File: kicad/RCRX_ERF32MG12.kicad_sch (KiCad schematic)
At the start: 90 parts, among them J20 USB_OTG, J21 USB, J22 USB, P10 LEDs, P6 SD Card, P9 BUZZ, SW1 SW_Push-switches, U1 MAX2650, U10 ATSAMD11D14A-M, U11 USB6B1, U12 MAX2650

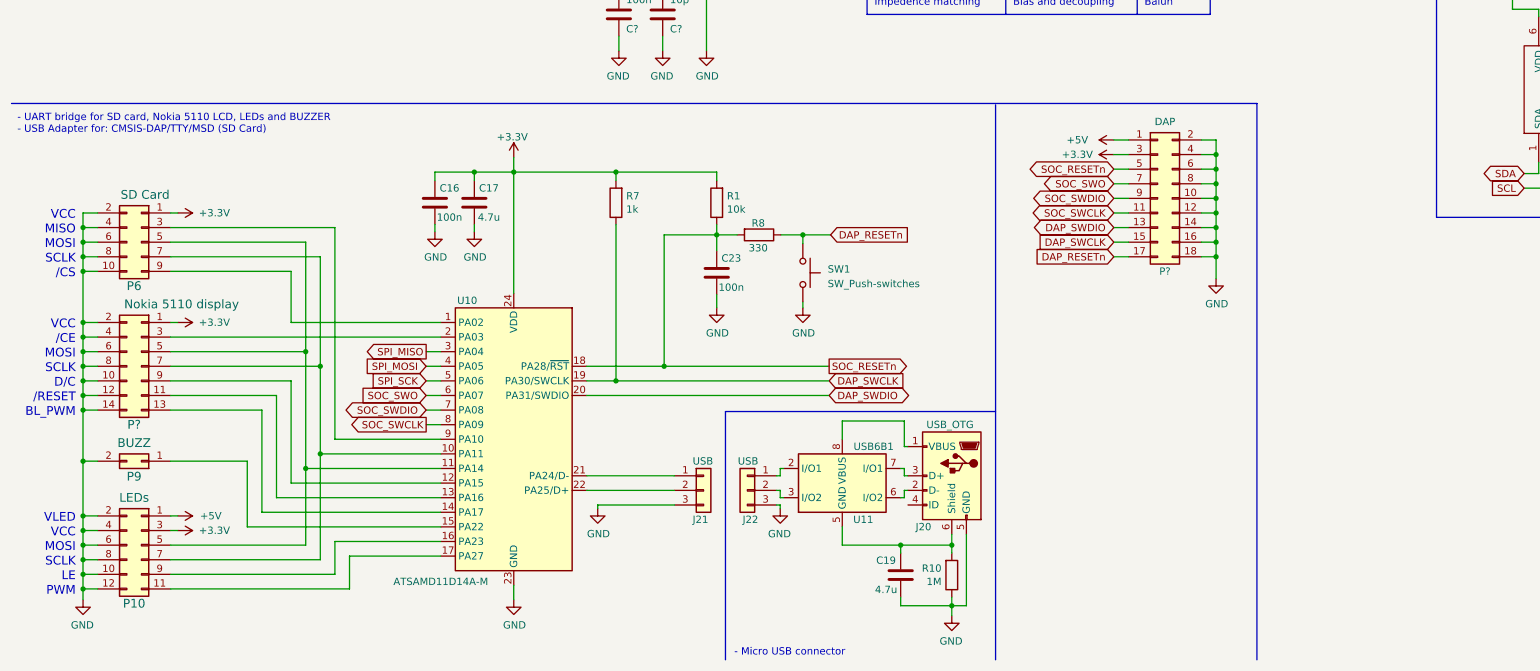
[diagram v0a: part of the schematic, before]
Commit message: Adding micro SD card slot in RX circuit
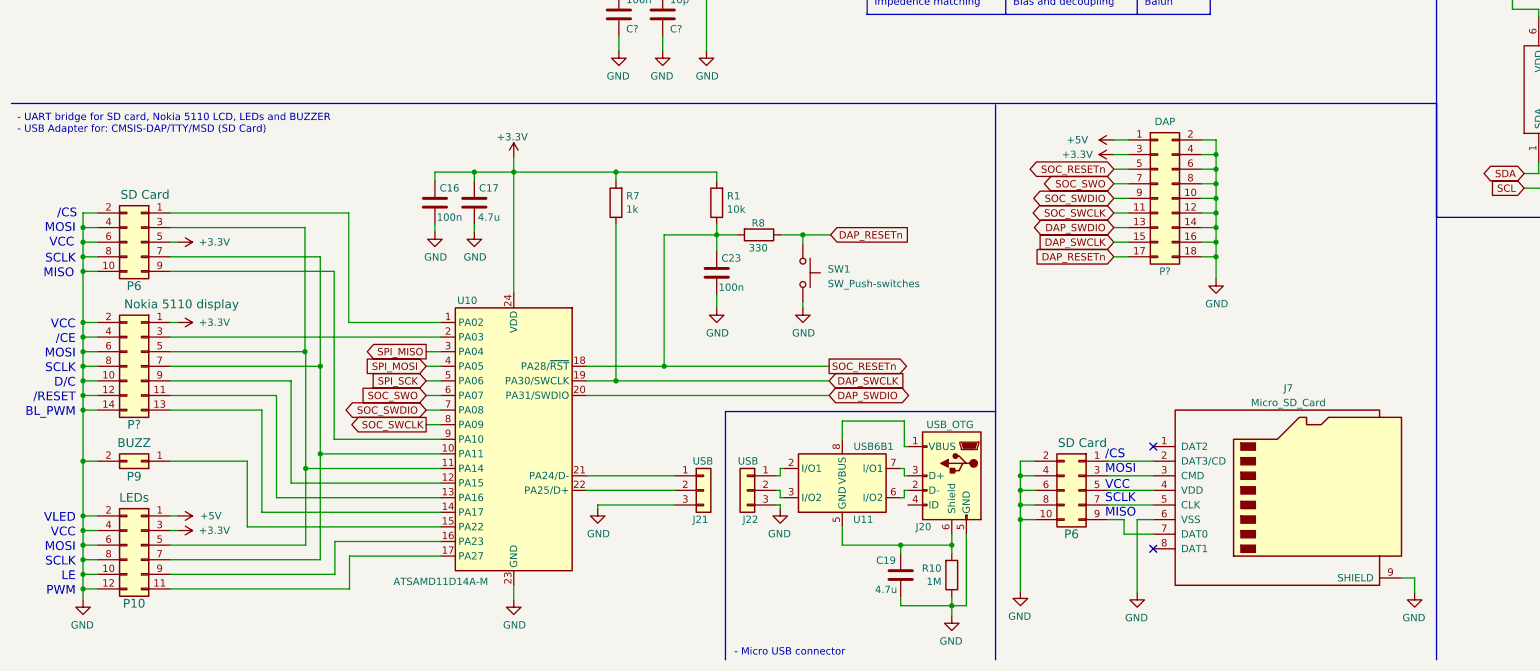
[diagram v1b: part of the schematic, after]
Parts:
- added J7: Micro_SD_Card, symbol Connector:Micro_SD_Card
- added P6: SD Card, symbol conn:Conn_02x05_Odd_Even
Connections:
- net +3V3: now also P6.5 (Pin_5); no longer P6.1 (Pin_1)
- net GND: now also J7.6 (VSS), J7.9 (SHIELD), P6.10 (Pin_10), P6.2 (Pin_2), P6.4 (Pin_4), P6.6 (Pin_6), P6.8 (Pin_8)
- net at U10.1 (PA02): now also P6.1 (Pin_1); no longer P6.9 (Pin_9)
- net at P10.5 (Pin_5), P?.5 (Pin_5), U10.11 (PA14): now also P6.3 (Pin_3); no longer P6.5 (Pin_5)
- net at U10.9 (PA10): now also P6.9 (Pin_9); no longer P6.3 (Pin_3)
- new net: J7.2 (DAT3/CD), P6.1 (Pin_1)
- new net: J7.3 (CMD), P6.3 (Pin_3)
- new net: J7.4 (VDD), P6.5 (Pin_5)
- new net: J7.5 (CLK), P6.7 (Pin_7)
- new net: J7.7 (DAT0), P6.9 (Pin_9)
- no-connect marks 11 -> 13

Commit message: Using EFM32HG310-QFN32 instead of SAMD11D14M for USB bridge - updating schematics
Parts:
- removed C23: 100n, symbol device:C
- removed J21, J22: USB, symbol Connector_Generic:Conn_01x03
- removed J7: Micro_SD_Card, symbol Connector:Micro_SD_Card
- removed P6 (x2): SD Card, symbol conn:Conn_02x05_Odd_Even
- removed P?: Nokia 5110 display, symbol Connector_Generic:Conn_02x07_Odd_Even
- removed R1: 10k, symbol device:R
- removed R7: 1k, symbol device:R
- removed R8: 330, symbol device:R
- removed U10: ATSAMD11D14A-M, Package_DFN_QFN:QFN-24-1EP_4x4mm_P0.5mm_EP2.6x2.6mm, symbol MCU_Microchip_SAMD:ATSAMD11D14A-M
- added C24, C32: 1u, symbol device:C
- added C25, C26: 10n, symbol device:C
- added C27, C28, C30: 0.1u, symbol device:C
- added C29, C31: 10u, symbol device:C
- added C33: 4.7u, symbol device:C
- added J11: Micro_SD_Card, symbol Connector:Micro_SD_Card
- added J21, J22: USB, symbol Connector_Generic:Conn_01x04
- added P?: Nokia 5110 display, symbol Connector_Generic:Conn_02x07_Odd_Even
- added U10: EFM32HG310F64G-C-QFN32, Package_DFN_QFN:QFN-32-1EP_6x6mm_P0.65mm_EP4.4x4.4mm, symbol EFM32HG310-QFN32:EFM32HG310F64G-C-QFN32
- C16: value 100n -> 10u
- C17: value 4.7u -> 0.1u
- SW1: value SW_Push-switches -> RESET
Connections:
- net +3V3: now also C25.2, C26.2, C27.2, C28.2, C29.2, C30.2, C31.2, J11.4 (VDD), P?.1 (Pin_1), U10.11 (AVDD_2), U10.14 (IOVDD_3), U10.15 (AVDD_0), U10.19 (VDD_DREG), U10.28 (IOVDD_5), U10.4 (IOVDD_0)
- net DAP_RESETn: now also U10.9 (~{RESET})
- net DAP_SWCLK: now also U10.25 (PF0)
- net DAP_SWDIO: now also U10.26 (PF1)
- net GND: now also C24.1, C25.1, C26.1, C27.1, C28.1, C29.1, C30.1, C31.1, C32.1, C33.1, J11.6 (VSS), J11.9 (SHIELD), J21.4 (Pin_4), J22.4 (Pin_4), P?.10 (Pin_10), P?.12 (Pin_12), P?.14 (Pin_14), P?.2 (Pin_2), P?.4 (Pin_4), P?.6 (Pin_6), P?.8 (Pin_8), U10.0 (VSS)
- net SOC_RESETn: now also U10.27 (PF2)
- net SOC_SWCLK: now also U10.10 (PB11)
- net SOC_SWDIO: now also U10.8 (PB8)
- net SOC_SWO: now also U10.7 (PB7)
- net SPI_MISO: now also U10.3 (PA2)
- net SPI_MOSI: now also U10.5 (PC0)
- net SPI_SCK: now also U10.6 (PC1)
- net at P10.7 (Pin_7): now also J11.5 (CLK), P?.7 (Pin_7), U10.13 (PB14)
- net at P10.5 (Pin_5): now also J11.3 (CMD), P?.5 (Pin_5), U10.16 (PD5)
- net at P9.1 (Pin_1): now also U10.30 (PE11)
- net at P10.9 (Pin_9): now also U10.31 (PE12)
- net at P10.11 (Pin_11): now also U10.32 (PE13)
- net at J20.1 (VBUS), U11.1 (VBUS), U11.8 (VBUS): now also J22.1 (Pin_1)
- net at U11.2 (I/O1): now also J22.2 (Pin_2)
- net at U11.3 (I/O2): now also J22.3 (Pin_3)
- new net: J11.2 (DAT3/CD), U10.1 (PA0)
- new net: J11.7 (DAT0), U10.12 (PB13)
- new net: P?.9 (Pin_9), U10.17 (PD6)
- new net: P?.11 (Pin_11), U10.18 (PD7)
- new net: P?.3 (Pin_3), U10.2 (PA1)
- new net: C24.2, U10.20 (DECOUPLE)
- new net: C33.2, J21.1 (Pin_1), U10.21 (USB_VREGI)
- new net: C32.2, U10.22 (USB_VREGO)
- new net: J21.3 (Pin_3), U10.23 (PC14/DM)
- new net: J21.2 (Pin_2), U10.24 (PC15/DP)
- new net: P?.13 (Pin_13), U10.29 (PE10)
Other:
- moved on the sheet: P?

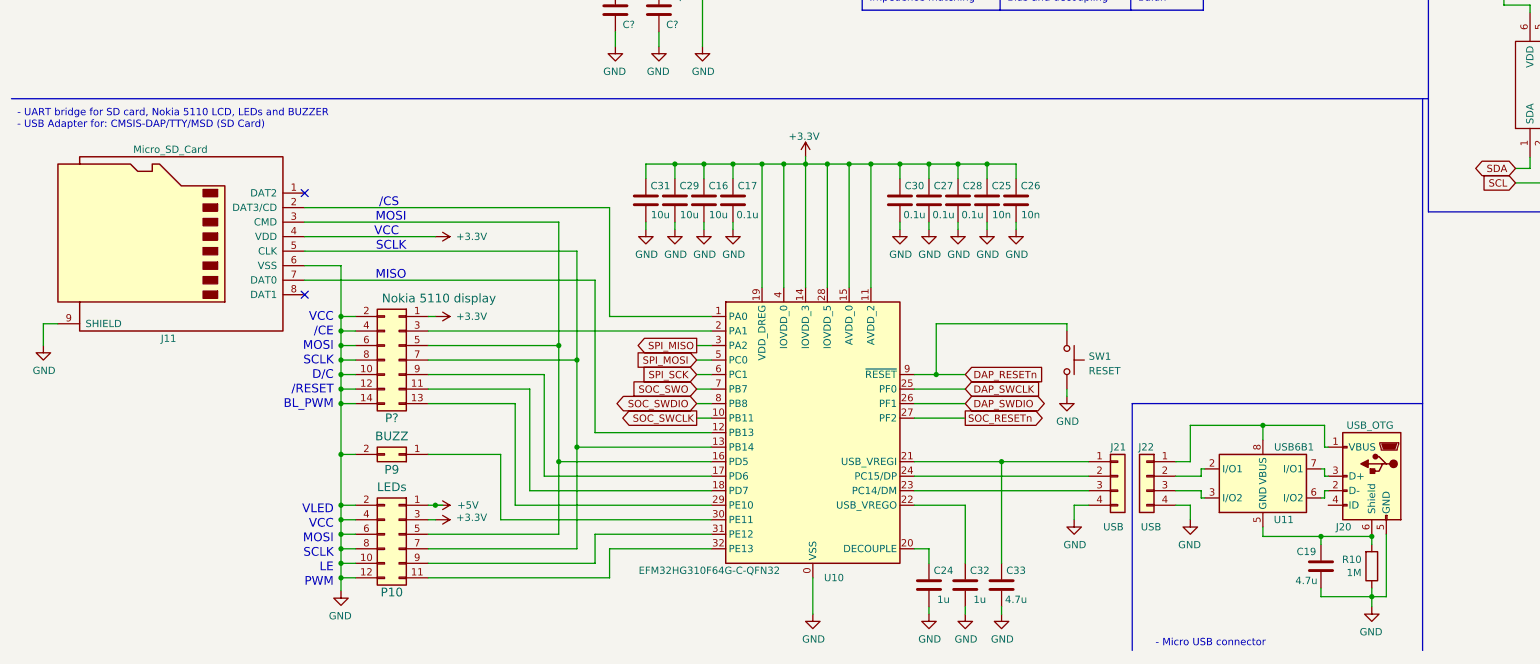
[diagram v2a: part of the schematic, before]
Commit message: Using 8x4 sqaure symbol for EFM32HG310-QFN32
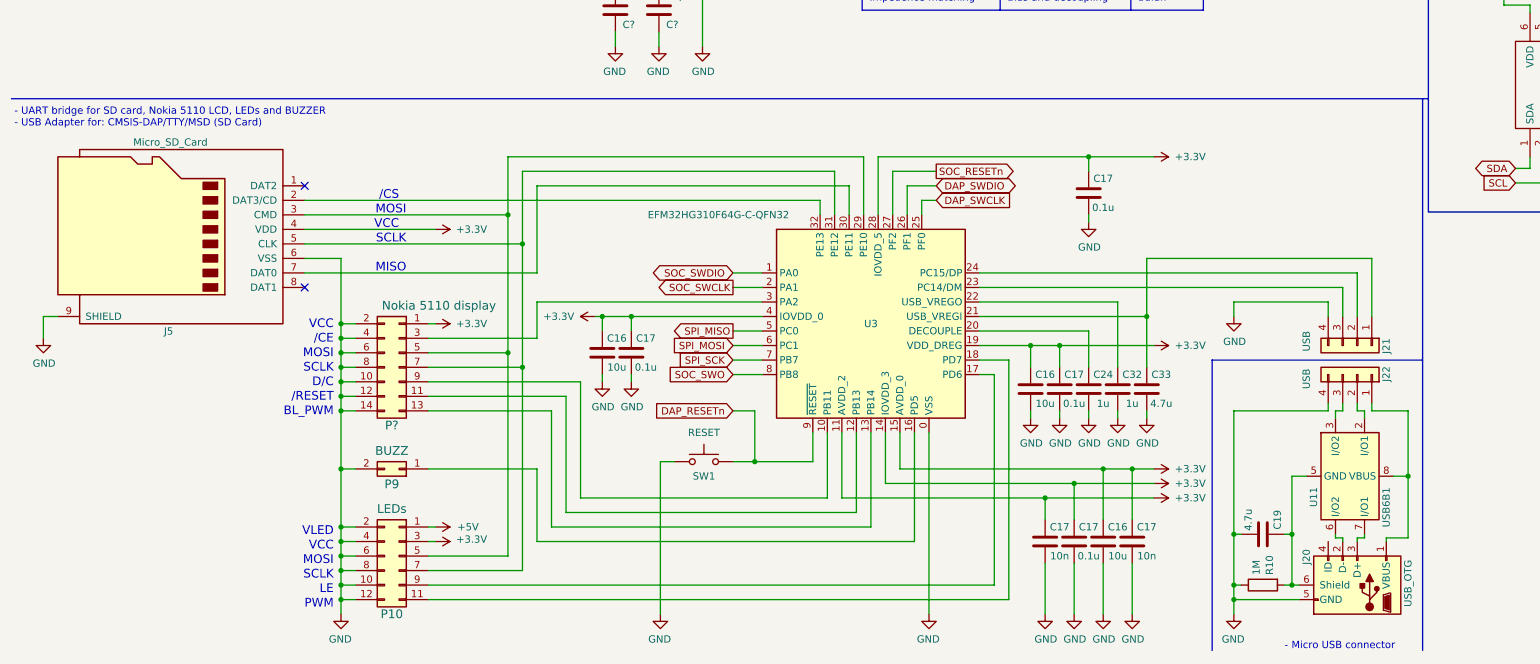
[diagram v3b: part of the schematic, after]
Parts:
- removed C16, C29, C31: 10u, symbol device:C
- removed C17, C27, C28, C30: 0.1u, symbol device:C
- removed C25, C26: 10n, symbol device:C
- removed J11: Micro_SD_Card, symbol Connector:Micro_SD_Card
- removed P?: Nokia 5110 display, symbol Connector_Generic:Conn_02x07_Odd_Even
- removed U10: EFM32HG310F64G-C-QFN32, Package_DFN_QFN:QFN-32-1EP_6x6mm_P0.65mm_EP4.4x4.4mm, symbol EFM32HG310-QFN32:EFM32HG310F64G-C-QFN32
- added C16 (x3): 10u, symbol device:C
- added C17 (x2): 10n, symbol device:C
- added C17 (x4): 0.1u, symbol device:C
- added J5: Micro_SD_Card, symbol Connector:Micro_SD_Card
- added P?: Nokia 5110 display, symbol Connector_Generic:Conn_02x07_Odd_Even
- added U3: EFM32HG310F64G-C-QFN32, Package_DFN_QFN:QFN-32-1EP_6x6mm_P0.65mm_EP4.4x4.4mm, symbol EFM32HG310-QFN32:EFM32HG310F64G-C-QFN32_1
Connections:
- net +3V3: now also C16.2, C16.2, C16.2, C17.2, C17.2, C17.2, C17.2, C17.2, C17.2, J5.4 (VDD), P?.1 (Pin_1), U3.11 (AVDD_2), U3.14 (IOVDD_3), U3.15 (AVDD_0), U3.19 (VDD_DREG), U3.28 (IOVDD_5), U3.4 (IOVDD_0)
- net DAP_RESETn: now also U3.9 (~{RESET})
- net DAP_SWCLK: now also U3.25 (PF0)
- net DAP_SWDIO: now also U3.26 (PF1)
- net GND: now also C16.1, C16.1, C16.1, C17.1, C17.1, C17.1, C17.1, C17.1, C17.1, J5.6 (VSS), J5.9 (SHIELD), P?.10 (Pin_10), P?.12 (Pin_12), P?.14 (Pin_14), P?.2 (Pin_2), P?.4 (Pin_4), P?.6 (Pin_6), P?.8 (Pin_8), U3.0 (VSS)
- net SOC_RESETn: now also U3.27 (PF2)
- net SOC_SWCLK: now also U3.2 (PA1)
- net SOC_SWDIO: now also U3.1 (PA0)
- net SOC_SWO: now also U3.8 (PB8)
- net SPI_MISO: now also U3.5 (PC0)
- net SPI_MOSI: now also U3.6 (PC1)
- net SPI_SCK: now also U3.7 (PB7)
- net at P10.11 (Pin_11): now also U3.18 (PD7)
- net at P10.5 (Pin_5): now also J5.3 (CMD), P?.5 (Pin_5), U3.29 (PE10)
- net at P10.7 (Pin_7): now also J5.5 (CLK), P?.7 (Pin_7), U3.31 (PE12)
- net at P10.9 (Pin_9): now also U3.17 (PD6)
- net at C24.2: now also U3.20 (DECOUPLE)
- net at C33.2, J21.1 (Pin_1): now also U3.21 (USB_VREGI)
- net at C32.2: now also U3.22 (USB_VREGO)
- net at J21.3 (Pin_3): now also U3.23 (PC14/DM)
- net at J21.2 (Pin_2): now also U3.24 (PC15/DP)
- net at P9.1 (Pin_1): now also U3.16 (PD5)
- new net: J5.2 (DAT3/CD), U3.32 (PE13)
- new net: J5.7 (DAT0), U3.30 (PE11)
- new net: P?.11 (Pin_11), U3.12 (PB13)
- new net: P?.13 (Pin_13), U3.13 (PB14)
- new net: P?.3 (Pin_3), U3.3 (PA2)
- new net: P?.9 (Pin_9), U3.10 (PB11)
